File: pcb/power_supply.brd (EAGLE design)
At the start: 57.8 x 66.4 mm, 53 parts, among them CON1 +, CON2 +, CON3 +, CON4 +, CON5 +, CON6 +, CON7 +, CON8 +, IC1 AP1507-D5-13, P1 2k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

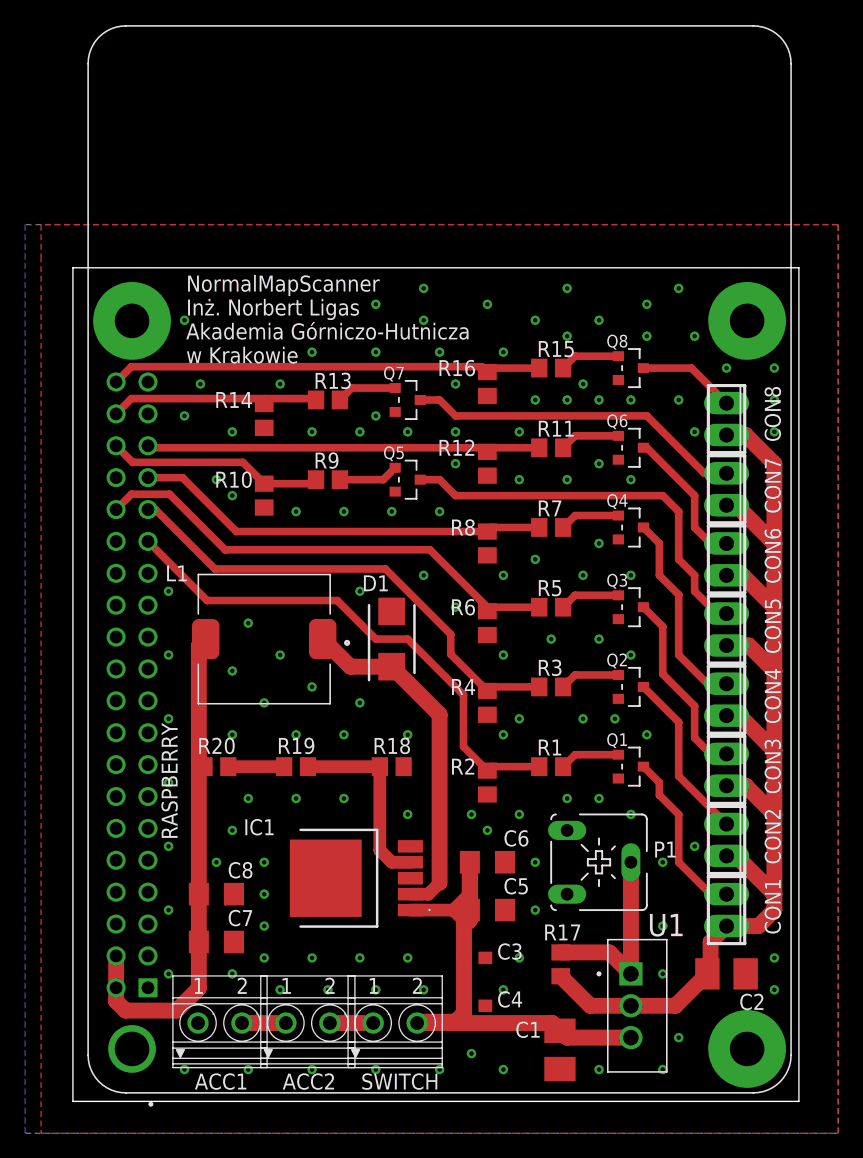
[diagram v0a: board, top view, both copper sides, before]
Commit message: pcb - gerber files, pcb ordered
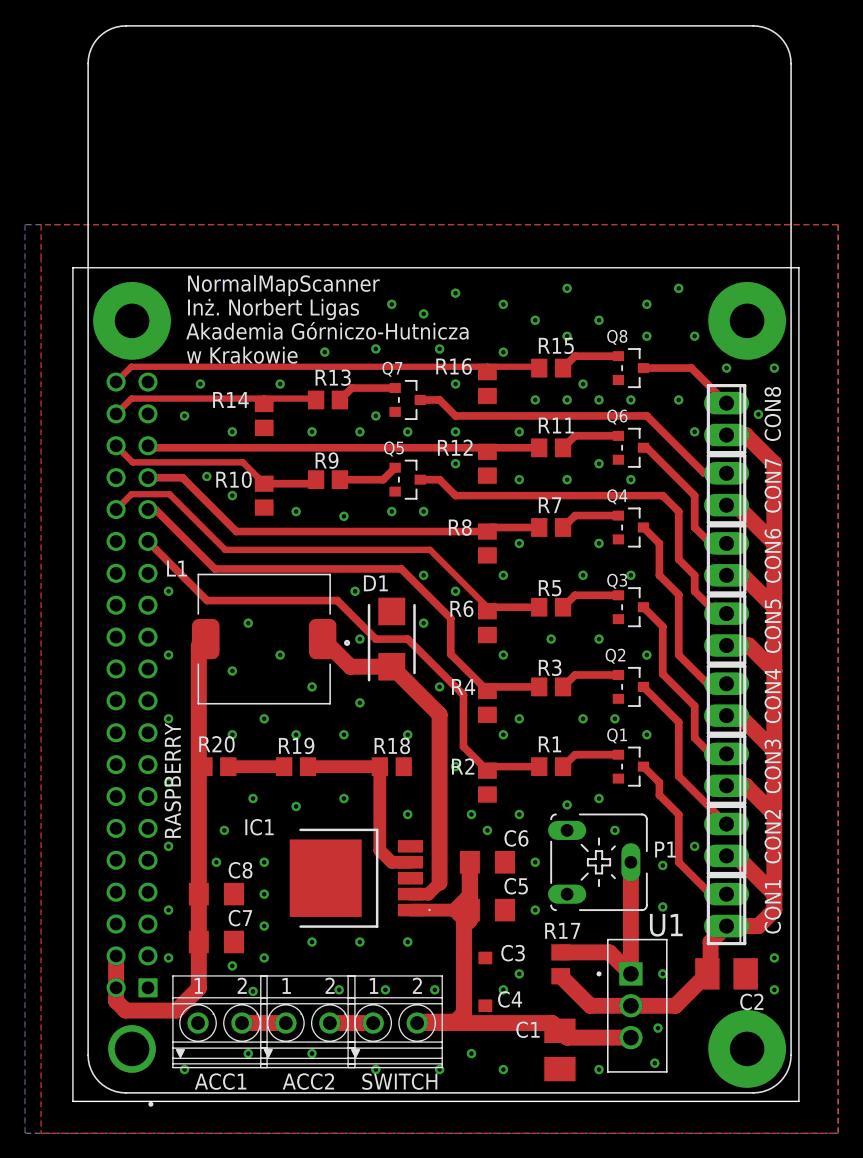
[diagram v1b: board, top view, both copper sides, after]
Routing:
- net N$20: track 38.2 -> 39.0 mm
